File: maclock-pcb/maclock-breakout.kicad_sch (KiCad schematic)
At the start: 19 parts, among them J1 B2B-ZR(LF)(SN), J2 B4B-ZR(LF)(SN), J3 B2B-ZR(LF)(SN), SW1 TSB001A3518A, SW2 TSB001A3518A, U1 PAM8302AASCR

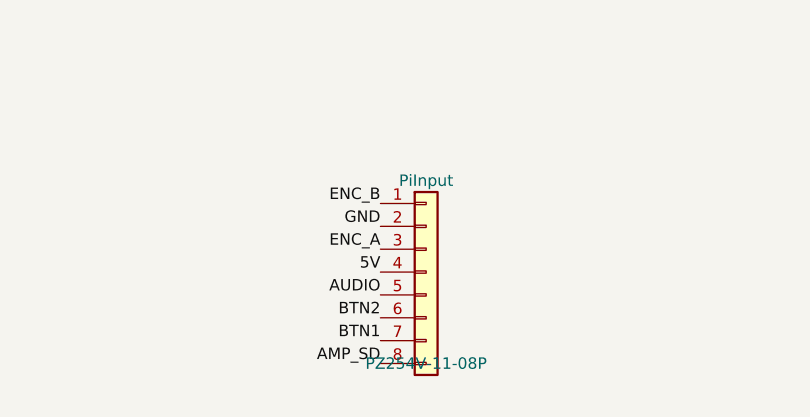
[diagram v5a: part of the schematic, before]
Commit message: Drop the MUTE header pin; PiInput back to 1x7
pinctrl on the running Maclock shows the Waveshare DPI overlay owns GPIO 0-9, 12-17, 20-25 and
10/11/18/19/26/27 are the dial, backlight, audio and buttons, so no header GPIO can drive the
amp's shutdown pin. R6 keeps it high (amp always on); the top-edge SD run, pad 8 and the MUTE
silk are removed. scripts/revert_mute_pin.py replays it from 1f01ab1. ERC 0, DRC 0/0.
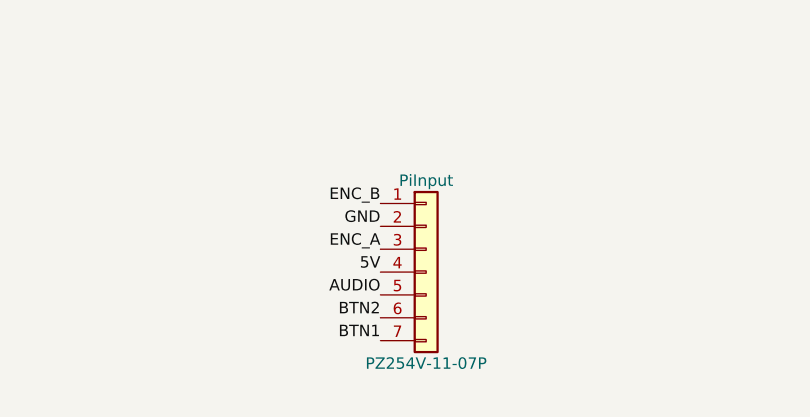
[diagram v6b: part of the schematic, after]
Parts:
- PiInput: value PZ254V-11-08P -> PZ254V-11-07P; footprint Connector_PinHeader_2.54mm:PinHeader_1x08_P2.54mm_Vertical -> Connector_PinHeader_2.54mm:PinHeader_1x07_P2.54mm_Vertical; symbol Connector_Generic:Conn_01x08 -> Connector_Generic:Conn_01x07; LCSC C492407 -> C492406
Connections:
- net AMP_SD: no longer PiInput.8 (Pin_8)
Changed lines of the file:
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@@
-		)
-	)
-	(label "AMP_SD"
-		(at 255.27 214.63 180)
-		(effects
-			(font
-				(size 1.27 1.27)
-			)
-			(justify right bottom)
 		)
 	)
@@
 	)
 	(symbol
-		(lib_id "Connector_Generic:Conn_01x08")
+		(lib_id "Connector_Generic:Conn_01x07")
 		(at 260.35 204.47 0)
 		(unit 1)
@@
 			)
 		)
-		(property "Value" "PZ254V-11-08P"
+		(property "Value" "PZ254V-11-07P"
 			(at 260.35 214.63 0)
 			(effects
@@
 			)
 		)
-		(property "Footprint" "Connector_PinHeader_2.54mm:PinHeader_1x08_P2.54mm_Vertical"
+		(property "Footprint" "Connector_PinHeader_2.54mm:PinHeader_1x07_P2.54mm_Vertical"
 			(at 260.35 204.47 0)
 			(hide yes)
@@
 			)
 		)
-		(property "LCSC" "C492407"
+		(property "LCSC" "C492406"
 			(at 260.35 204.47 0)
 			(hide yes)

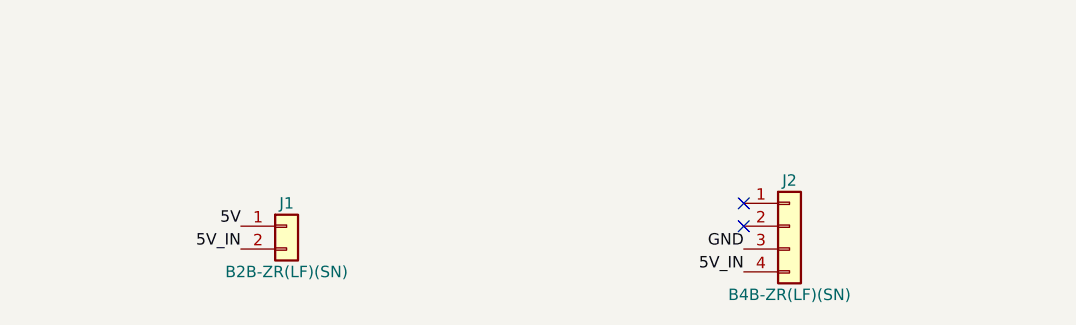
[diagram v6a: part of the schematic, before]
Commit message: J1/J2: JST SH 1.0 mm SMD (BM02B/BM04B-SRSS-TB) to take the Maclock's own plugs
The stock Maclock power and switch harnesses end in 1.0 mm blade-style
plugs (JST SH), not the 1.5 mm ZH the board carried. Swap J1 -> BM02B-SRSS-TB
(C160388) and J2 -> BM04B-SRSS-TB (C160390), both top-entry SMD on B.Cu at
the same spots on the bottom edge, pad 1 still nearest J1, pads facing the
edge and the MP tabs toward the board.

Re-routed the two nets the swap disturbed: 5V drops from the y=98 trunk
between J1's tabs into pad 1; 5V_IN leaves J1 pad 2, runs west at y=101.9
(above SW2's locator holes, which sit in the edge lane), and drops to the
edge lane only west of x=152.5 to reach J2 pad 4. J2's +/- silk moved under
its pads. ERC 0, DRC 0 errors / 0 unconnected (the two pre-existing
warnings remain). J3 (speaker) stays ZH for now.
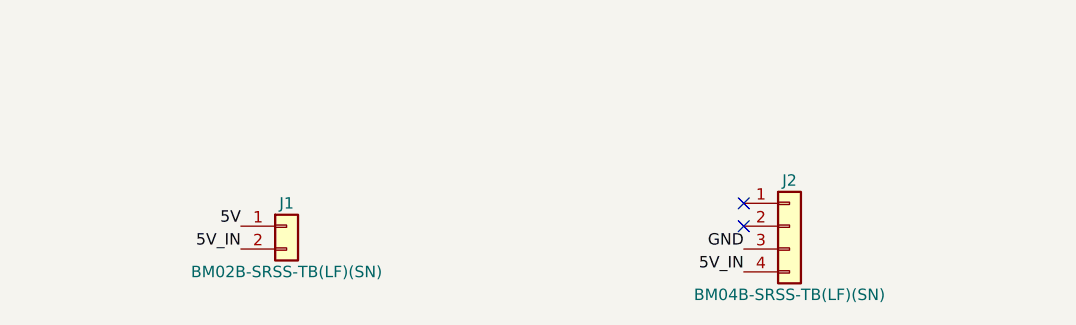
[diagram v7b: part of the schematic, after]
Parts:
- J1: value B2B-ZR(LF)(SN) -> BM02B-SRSS-TB(LF)(SN); footprint Connector_JST:JST_ZH_B2B-ZR_1x02_P1.50mm_Vertical -> Connector_JST:JST_SH_BM02B-SRSS-TB_1x02-1MP_P1.00mm_Vertical; LCSC C158011 -> C160388
- J2: value B4B-ZR(LF)(SN) -> BM04B-SRSS-TB(LF)(SN); footprint Connector_JST:JST_ZH_B4B-ZR_1x04_P1.50mm_Vertical -> Connector_JST:JST_SH_BM04B-SRSS-TB_1x04-1MP_P1.00mm_Vertical; LCSC C157997 -> C160390
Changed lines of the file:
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@@
 			)
 		)
-		(property "Value" "B2B-ZR(LF)(SN)"
+		(property "Value" "BM02B-SRSS-TB(LF)(SN)"
 			(at 119.38 214.63 0)
 			(effects
@@
 			)
 		)
-		(property "Footprint" "Connector_JST:JST_ZH_B2B-ZR_1x02_P1.50mm_Vertical"
+		(property "Footprint" "Connector_JST:JST_SH_BM02B-SRSS-TB_1x02-1MP_P1.00mm_Vertical"
 			(at 119.38 209.55 0)
 			(hide yes)
@@
 			)
 		)
-		(property "LCSC" "C158011"
+		(property "LCSC" "C160388"
 			(at 119.38 209.55 0)
 			(hide yes)
@@
 			)
 		)
-		(property "Value" "B4B-ZR(LF)(SN)"
+		(property "Value" "BM04B-SRSS-TB(LF)(SN)"
 			(at 175.26 217.17 0)
 			(effects
@@
 			)
 		)
-		(property "Footprint" "Connector_JST:JST_ZH_B4B-ZR_1x04_P1.50mm_Vertical"
+		(property "Footprint" "Connector_JST:JST_SH_BM04B-SRSS-TB_1x04-1MP_P1.00mm_Vertical"
 			(at 175.26 209.55 0)
 			(hide yes)
@@
 			)
 		)
-		(property "LCSC" "C157997"
+		(property "LCSC" "C160390"
 			(at 175.26 209.55 0)
 			(hide yes)
